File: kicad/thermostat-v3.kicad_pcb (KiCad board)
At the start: 2 copper layers, 140 x 64 mm, 100 parts, among them J1 HVAC R C W Y G, J2 USB-C, J3 Stemma QT, J4 2.9in EPD FPC, Q1 AO3400A, Q2 T435-600B, Q3 T435-600B, Q4 T435-600B, SW1 RESET, SW2 BOOT, SW3 UP, SW4 DOWN, SW5 MODE, U1 LMR16006XDDCR, U2 USBLC6-2SC6, U3 ESP32-C6-WROOM-1-N8, U4 STWD100NYWY3F, U5 SHT40-AD1B, U6 MOC3063S, U7 MOC3063S, U8 MOC3063S

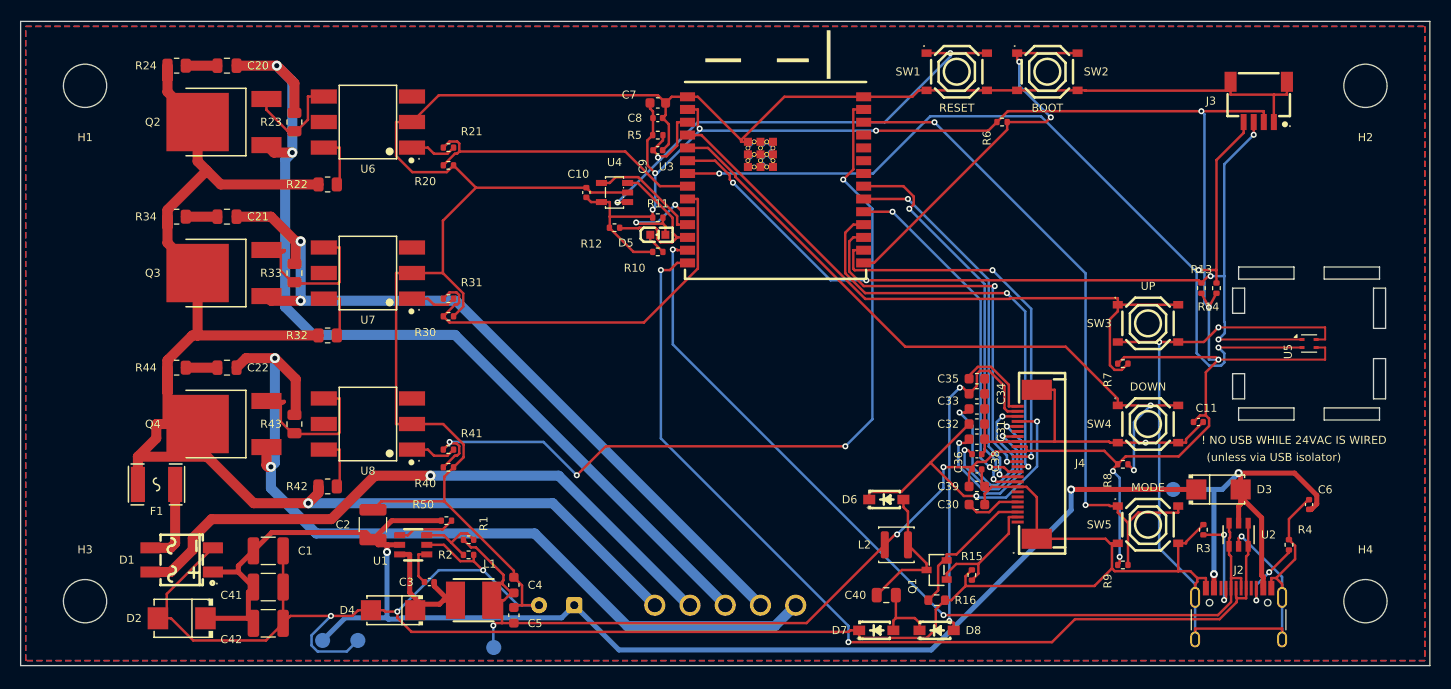
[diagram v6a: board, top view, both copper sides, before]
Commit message: Rev 9: R51 3.3R pulse-proof series resistor (bridge->bulk, TVS clamp ~58V at U1), L1 SWPA6045S220MT 22uH Isat 2.2A; regenerated fab (DRC/ERC 0); final review notes; exploded case+PCB renders
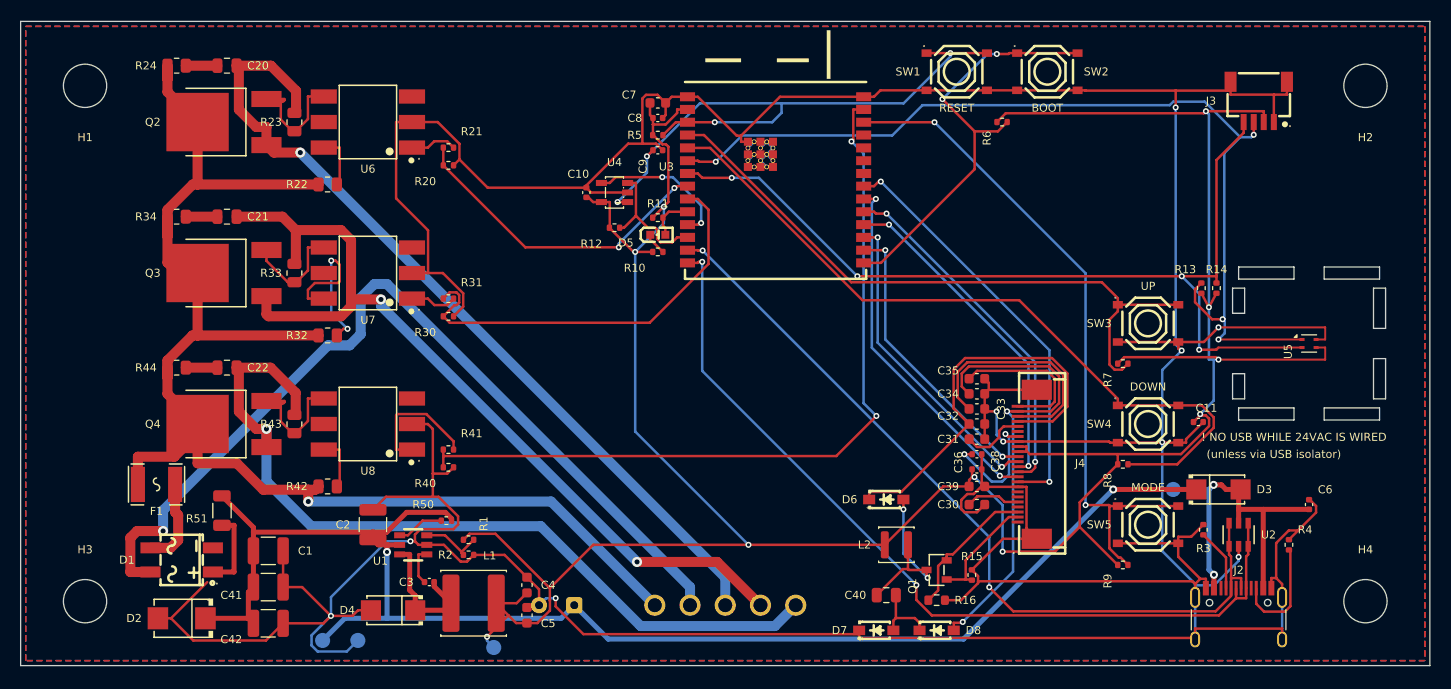
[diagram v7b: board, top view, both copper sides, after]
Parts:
- added R51: 3.3R 0.75W pulse, Resistor_SMD:R_1206_3216Metric, F.Cu at (120.0, 148.6)
- L1: footprint tstat:L_4030_SWPA -> Inductor_SMD:L_Sunlord_SWPA6045S
- moved C4 1.30 mm to (150.3, 156.0)
- moved C5 1.30 mm to (150.3, 159.0)
- moved L1 0.30 mm to (145.0, 157.8)
- turned R50 to 180 degrees
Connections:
- D1 pad 1: VIN_HV -> VIN_RECT
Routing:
- net HVAC_C: track 63.6 -> 89.1 mm
- net +3V3: track 265.2 -> 284.6 mm, vias 12 -> 10
- net OPTO_MT2_Y: track 5.56 -> 17.9 mm, vias 0 -> 2
- net EPD_VSH1: track 17.9 -> 6.36 mm, vias 2 -> 0
- net USB_DP: track 97.7 -> 86.6 mm
- net EPD_VGL: track 35.5 -> 45.8 mm
- net HVAC_Y: track 77.5 -> 86.8 mm
- net EPD_MOSI: track 38.2 -> 29.0 mm
- net EPD_CS: track 42.3 -> 33.3 mm
- net GND: track 548.8 -> 557.4 mm, vias 7 -> 10
- net OPTO_A_G: track 4.63 -> 12.7 mm
- net HVAC_W: track 93.2 -> 85.2 mm, vias 2 -> 1
- net VIN_RECT: track 0.00 -> 7.94 mm
- net I2C_SCL: track 100.0 -> 92.2 mm, vias 3 -> 4
- net EPD_SCK: track 38.8 -> 31.1 mm
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
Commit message: Rev 10: L1 moved off the EPD footprint (buck stage shifted left, hot loop ~6 mm^2), protected pre-routes; case +2 mm standoffs, pocket/notch removed, lip 5.5, panel_gap 5.0; fit check, STL/3MF/renders regenerated
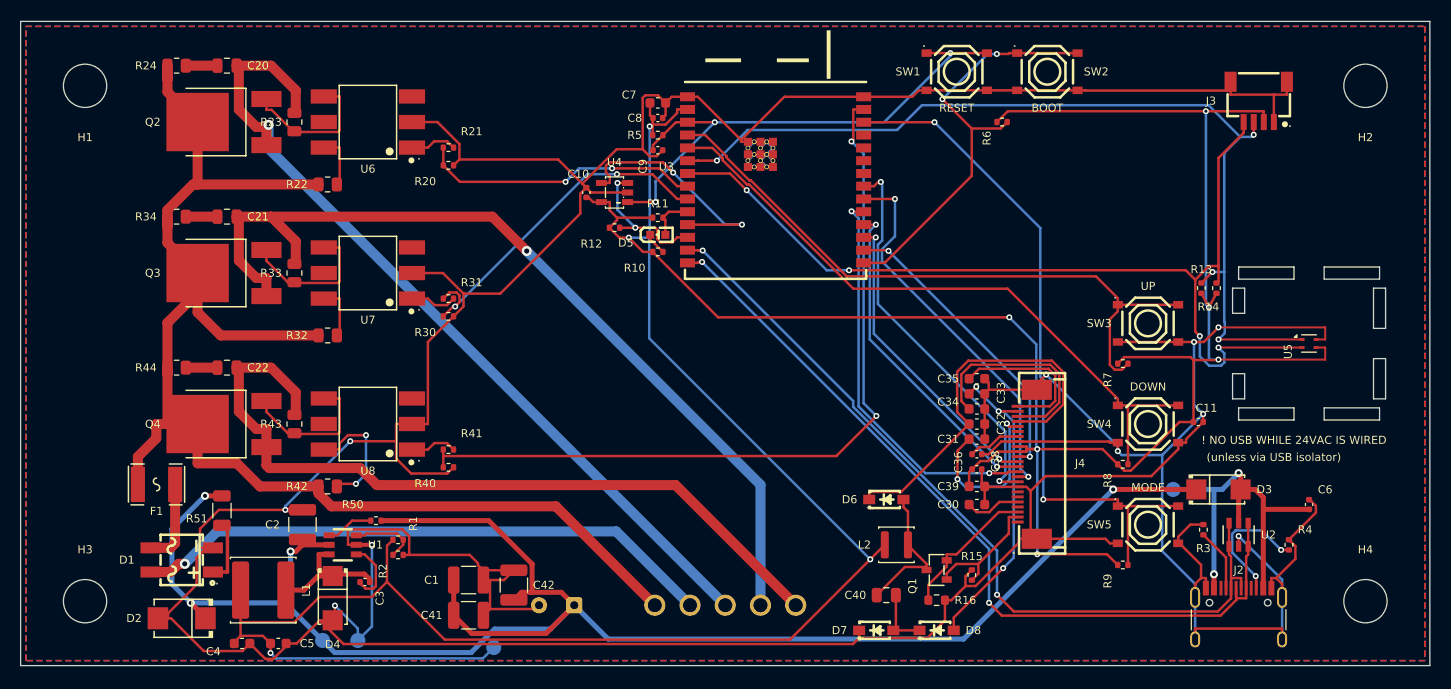
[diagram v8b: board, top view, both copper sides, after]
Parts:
- moved C4 28.9 mm to (122.0, 161.8), turned to 0 degrees
- moved C5 24.9 mm to (125.6, 161.8), turned to 0 degrees
- moved C42 24.7 mm to (149.0, 156.0), turned to 90 degrees
- moved L1 20.9 mm to (124.1, 156.5), turned to 180 degrees
- moved C1 20.1 mm to (144.5, 155.5)
- moved C41 20.1 mm to (144.5, 159.0)
- moved C2 7.00 mm to (128.0, 150.0)
- moved R1 7.00 mm to (137.5, 151.5)
- moved R2 7.00 mm to (137.5, 153.0)
- moved R50 7.00 mm to (135.3, 149.6)
- moved U1 7.00 mm to (132.0, 152.0)
- moved C3 6.40 mm to (134.2, 155.7)
- moved D4 6.12 mm to (131.0, 157.3), turned to -90 degrees
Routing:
- net +3V3: track 284.6 -> 371.9 mm
- net VIN_HV: track 146.3 -> 181.9 mm, vias 2 -> 4
- net HVAC_C: track 89.1 -> 58.3 mm
- net EPD_VGL: track 45.8 -> 31.4 mm, vias 2 -> 3
- net OPTO_MT2_Y: track 17.9 -> 5.56 mm, vias 2 -> 0
- net EPD_VSH1: track 6.36 -> 17.2 mm, vias 0 -> 2
- net WD_WDI: track 14.5 -> 24.3 mm
- net BTN_DOWN: track 74.8 -> 65.7 mm
- net ESP_EN: track 61.8 -> 53.1 mm, vias 4 -> 3
- net GND: track 557.4 -> 565.8 mm
- net OPTO_A_G: track 12.7 -> 4.67 mm
- net DRV_Y: track 41.8 -> 34.4 mm, vias 0 -> 2
- net EPD_VDD: track 12.1 -> 5.26 mm, vias 2 -> 0
- net OPTO_MT2_G: track 5.56 -> 12.4 mm, vias 0 -> 2
- net HVAC_G: track 83.6 -> 79.2 mm, vias 1 -> 0
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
